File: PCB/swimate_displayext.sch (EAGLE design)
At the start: 56 parts, among them IC1 LPC11U24, T1 BSS84, T2 BSS84, U1 USD-SOCKETNEW, U3 NC7SV86P5X, U5 DS3231MZ/V+T, U6 MAX1595EUA33+, U7 MAX1811ESA-T, U8 MAX16054AZT+T, U9 HC_05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

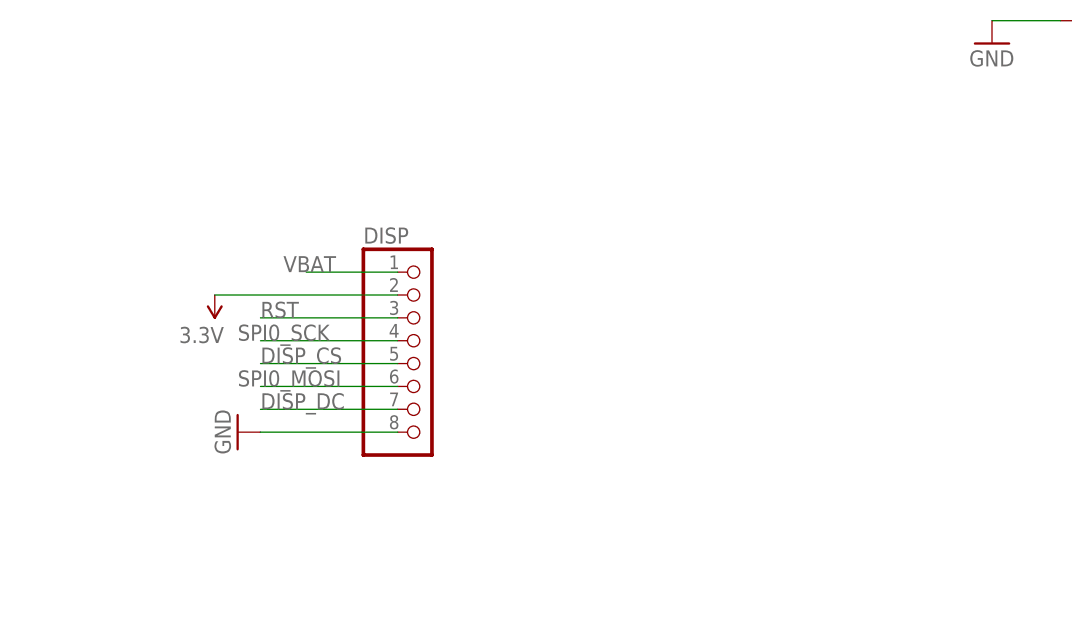
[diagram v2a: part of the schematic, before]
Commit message: Displayboard completed.. Need to check connector width
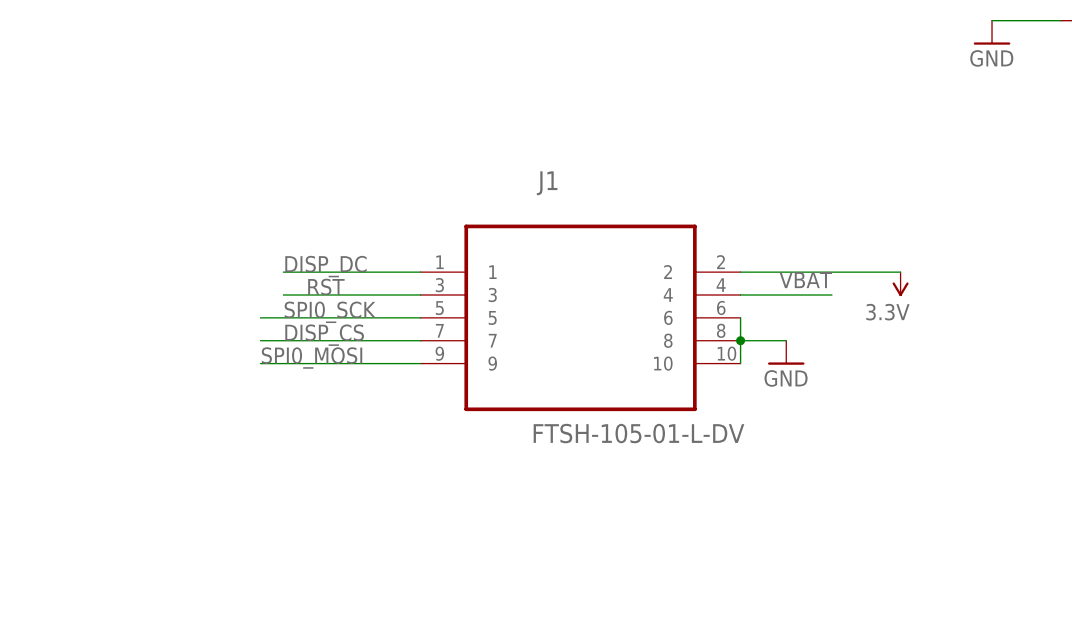
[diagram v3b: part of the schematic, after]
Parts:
- removed DISP: (no value), microbuilder:JST_8PIN
- added J1: FTSH-105-01-L-DV, SAMTEC-HTSW-FTxx_By_element14_Batch_1:FTSH-105-01-L-DV
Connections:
- net 3.3V: now also J1.2; no longer DISP.2
- net DISP_CS: now also J1.7; no longer DISP.5
- net DISP_DC: now also J1.1; no longer DISP.7
- net GND: now also J1.10, J1.6, J1.8; no longer DISP.8
- net RST: now also J1.3; no longer DISP.3
- net SPI0_MOSI: now also J1.9; no longer DISP.6
- net SPI0_SCK: now also J1.5; no longer DISP.4
- net VBAT: now also J1.4; no longer DISP.1
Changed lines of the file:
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@@
 <part name="R1" library="SparkFun-Passives" deviceset="RESISTOR" device="0603-RES" value="10k"/>
 <part name="R13" library="SparkFun-Passives" deviceset="RESISTOR" device="0603-RES" value="24k"/>
-<part name="DISP" library="microbuilder" deviceset="JST_8PIN" device=""/>
 <part name="SUPPLY1" library="SparkFun-Aesthetics" deviceset="3.3V" device=""/>
 <part name="GND4" library="SparkFun-Aesthetics" deviceset="GND" device=""/>
@@
 <part name="U3" library="Fairchild_By_element14_Batch_1" deviceset="NC7SV86P5X" device=""/>
 <part name="GND33" library="SparkFun-Aesthetics" deviceset="GND" device=""/>
+<part name="J1" library="SAMTEC-HTSW-FTxx_By_element14_Batch_1" deviceset="FTSH-105-01-L-DV" device=""/>
 </parts>
 <sheets>
@@
 <instance part="R1" gate="G$1" x="-205.74" y="15.24" rot="R90"/>
 <instance part="R13" gate="G$1" x="-205.74" y="-10.16" rot="R90"/>
-<instance part="DISP" gate="G$1" x="-142.24" y="-50.8"/>
-<instance part="SUPPLY1" gate="G$1" x="-165.1" y="-43.18" rot="R180"/>
-<instance part="GND4" gate="1" x="-162.56" y="-58.42" rot="R270"/>
+<instance part="SUPPLY1" gate="G$1" x="-88.9" y="-40.64" rot="R180"/>
+<instance part="GND4" gate="1" x="-101.6" y="-50.8"/>
 <instance part="GND3" gate="1" x="139.7" y="66.04"/>
 <instance part="SUPPLY11" gate="G$1" x="114.3" y="81.28" rot="R180"/>
@@
 <instance part="U3" gate="A" x="-213.36" y="83.82"/>
 <instance part="GND33" gate="1" x="-236.22" y="71.12"/>
+<instance part="J1" gate="A" x="-124.46" y="-43.18"/>
 </instances>
 <busses>
@@
 </segment>
 <segment>
-<pinref part="DISP" gate="G$1" pin="1"/>
-<wire x1="-144.78" y1="-40.64" x2="-154.94" y2="-40.64" width="0.1524" layer="91"/>
-<label x="-157.48" y="-40.64" size="1.778" layer="95"/>
-</segment>
-<segment>
 <pinref part="U8" gate="A" pin="VCC"/>
 <label x="-256.54" y="119.38" size="1.778" layer="95"/>
@@
 <wire x1="-231.14" y1="86.36" x2="-238.76" y2="86.36" width="0.1524" layer="91"/>
 <label x="-238.76" y="86.36" size="1.778" layer="95"/>
+</segment>
+<segment>
+<pinref part="J1" gate="A" pin="4"/>
+<wire x1="-106.68" y1="-43.18" x2="-96.52" y2="-43.18" width="0.1524" layer="91"/>
+<label x="-96.52" y="-40.64" size="1.778" layer="95" rot="R180"/>
 </segment>
 </net>
@@
 </segment>
 <segment>
-<pinref part="DISP" gate="G$1" pin="8"/>
-<wire x1="-144.78" y1="-58.42" x2="-160.02" y2="-58.42" width="0.1524" layer="91"/>
-<pinref part="GND4" gate="1" pin="GND"/>
-</segment>
-<segment>
 <pinref part="U2" gate="G$1" pin="CLKIN"/>
 <pinref part="U2" gate="G$1" pin="FSYNC"/>
@@
 <wire x1="-236.22" y1="73.66" x2="-231.14" y2="73.66" width="0.1524" layer="91"/>
 </segment>
+<segment>
+<pinref part="J1" gate="A" pin="6"/>
+<pinref part="J1" gate="A" pin="8"/>
+<wire x1="-106.68" y1="-45.72" x2="-106.68" y2="-48.26" width="0.1524" layer="91"/>
+<pinref part="J1" gate="A" pin="10"/>
+<wire x1="-106.68" y1="-48.26" x2="-106.68" y2="-50.8" width="0.1524" layer="91"/>
+<junction x="-106.68" y="-48.26"/>
+<wire x1="-106.68" y1="-48.26" x2="-101.6" y2="-48.26" width="0.1524" layer="91"/>
+<pinref part="GND4" gate="1" pin="GND"/>
+</segment>
 </net>
 <net name="3.3V" class="0">
@@
 <pinref part="SUPPLY10" gate="G$1" pin="3.3V"/>
 <wire x1="73.66" y1="-10.16" x2="73.66" y2="-15.24" width="0.1524" layer="91"/>
-</segment>
-<segment>
-<pinref part="DISP" gate="G$1" pin="2"/>
-<pinref part="SUPPLY1" gate="G$1" pin="3.3V"/>
-<wire x1="-144.78" y1="-43.18" x2="-165.1" y2="-43.18" width="0.1524" layer="91"/>
 </segment>
 <segment>
@@
 <junction x="-58.42" y="114.3"/>
 </segment>
+<segment>
+<pinref part="J1" gate="A" pin="2"/>
+<pinref part="SUPPLY1" gate="G$1" pin="3.3V"/>
+<wire x1="-106.68" y1="-40.64" x2="-88.9" y2="-40.64" width="0.1524" layer="91"/>
+</segment>
 </net>
 <net name="VUSB" class="0">
@@
 </segment>
 <segment>
-<pinref part="DISP" gate="G$1" pin="6"/>
-<wire x1="-144.78" y1="-53.34" x2="-160.02" y2="-53.34" width="0.1524" layer="91"/>
-<label x="-162.56" y="-53.34" size="1.778" layer="95"/>
+<wire x1="-142.24" y1="-50.8" x2="-160.02" y2="-50.8" width="0.1524" layer="91"/>
+<label x="-160.02" y="-50.8" size="1.778" layer="95"/>
+<pinref part="J1" gate="A" pin="9"/>
 </segment>
 </net>
@@
 </segment>
 <segment>
-<pinref part="DISP" gate="G$1" pin="4"/>
-<wire x1="-144.78" y1="-48.26" x2="-160.02" y2="-48.26" width="0.1524" layer="91"/>
-<label x="-162.56" y="-48.26" size="1.778" layer="95"/>
+<wire x1="-142.24" y1="-45.72" x2="-160.02" y2="-45.72" width="0.1524" layer="91"/>
+<label x="-157.48" y="-45.72" size="1.778" layer="95"/>
+<pinref part="J1" gate="A" pin="5"/>
 </segment>
 <segment>
@@
 </segment>
 <segment>
-<wire x1="-144.78" y1="-45.72" x2="-160.02" y2="-45.72" width="0.1524" layer="91"/>
-<label x="-160.02" y="-45.72" size="1.778" layer="95"/>
-<pinref part="DISP" gate="G$1" pin="3"/>
+<label x="-154.94" y="-43.18" size="1.778" layer="95"/>
+<pinref part="J1" gate="A" pin="3"/>
+<wire x1="-142.24" y1="-43.18" x2="-157.48" y2="-43.18" width="0.1524" layer="91"/>
 </segment>
 </net>
@@
 <net name="DISP_CS" class="0">
 <segment>
-<pinref part="DISP" gate="G$1" pin="5"/>
-<wire x1="-144.78" y1="-50.8" x2="-160.02" y2="-50.8" width="0.1524" layer="91"/>
-<label x="-160.02" y="-50.8" size="1.778" layer="95"/>
+<label x="-157.48" y="-48.26" size="1.778" layer="95"/>
+<pinref part="J1" gate="A" pin="7"/>
+<wire x1="-142.24" y1="-48.26" x2="-160.02" y2="-48.26" width="0.1524" layer="91"/>
 </segment>
 <segment>
@@
 <net name="DISP_DC" class="0">
 <segment>
-<pinref part="DISP" gate="G$1" pin="7"/>
-<wire x1="-144.78" y1="-55.88" x2="-160.02" y2="-55.88" width="0.1524" layer="91"/>
-<label x="-160.02" y="-55.88" size="1.778" layer="95"/>
-</segment>
-<segment>
+<wire x1="-142.24" y1="-40.64" x2="-157.48" y2="-40.64" width="0.1524" layer="91"/>
+<label x="-157.48" y="-40.64" size="1.778" layer="95"/>
+<pinref part="J1" gate="A" pin="1"/>
+</segment>
+<segment>

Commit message: display board update
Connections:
- net GND: no longer J1.6
- net SPI0_MISO: now also J1.6
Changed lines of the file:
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@@
 </segment>
 <segment>
-<pinref part="J1" gate="A" pin="6"/>
 <pinref part="J1" gate="A" pin="8"/>
-<wire x1="-106.68" y1="-45.72" x2="-106.68" y2="-48.26" width="0.1524" layer="91"/>
 <pinref part="J1" gate="A" pin="10"/>
 <wire x1="-106.68" y1="-48.26" x2="-106.68" y2="-50.8" width="0.1524" layer="91"/>
@@
 <label x="-50.8" y="48.26" size="1.778" layer="95"/>
 </segment>
-</net>
+<segment>
+<pinref part="J1" gate="A" pin="6"/>
+<wire x1="-106.68" y1="-45.72" x2="-96.52" y2="-45.72" width="0.1524" layer="91"/>
+<label x="-106.68" y="-45.72" size="1.778" layer="95"/>
+</segment>
+</net>

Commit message: Added top and bottom ground and power planes
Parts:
- removed R9: 24K, SparkFun-Passives:RESISTOR0805-RES
- added R2: 24k, SparkFun-Passives:RESISTOR0805-RES
- added SJ6: (no value), SparkFun-Passives:SOLDERJUMPER_2WAYS
- U3: value NC7SV86P5X -> NC7SZ32M5; device Fairchild_By_element14_Batch_1:NC7SV86P5X -> Fairchild_By_element14_Batch_1:NC7SZ32M5
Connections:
- removed net N$2: U3.A, U8.OUT
- removed net SPI_MOSI0: JTAG1.6
- new net BT_RST: IC1.PIO1.16/RI/CT16B0C0, U9.RST
- new net DISP_RST: IC1.PIO1.6, J1.3
- new net DISP_SW: IC1.PIO1.3/CT32B1M3, J1.8
- new net N$3: SJ6.2, U7.SELI
- new net SW_PWR_STATE: IC1.PIO1.11, U3.A, U8.OUT
- net 3.3V: now also T2.S; no longer T2.D
- net DISP_CS: now also IC1.PIO1.0/CT32B1M0; no longer IC1.PIO1.25/CT32B0M1
- net DISP_DC: now also IC1.PIO1.25/CT32B0M1; no longer IC1.PIO1.0/CT32B1M0
- net GND: now also R2.2, SJ6.1; no longer J1.8, R9.2, U7.SELI
- net MPU_INT: now also IC1.PIO1.4/CT32B1C0
- net N$15: now also T2.D; no longer R9.1, T2.S
- net PO_DISABLE: now also R2.1
- net RST: no longer J1.3, U9.RST
- net SPI0_MOSI: now also JTAG1.6
- net VBAT: now also SJ6.3
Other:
- moved on the sheet: T2
